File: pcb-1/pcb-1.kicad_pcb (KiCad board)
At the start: 2 copper layers, 131 x 74 mm, 8 parts, among them J1 Raspberry_Pi_2_3, J2 Screw_Terminal_01x03, J3 Conn_01x07_Socket, J4 Screw_Terminal_01x02, J5 Conn_01x02_Socket, U1 Pico, U2 TSR 2-2450

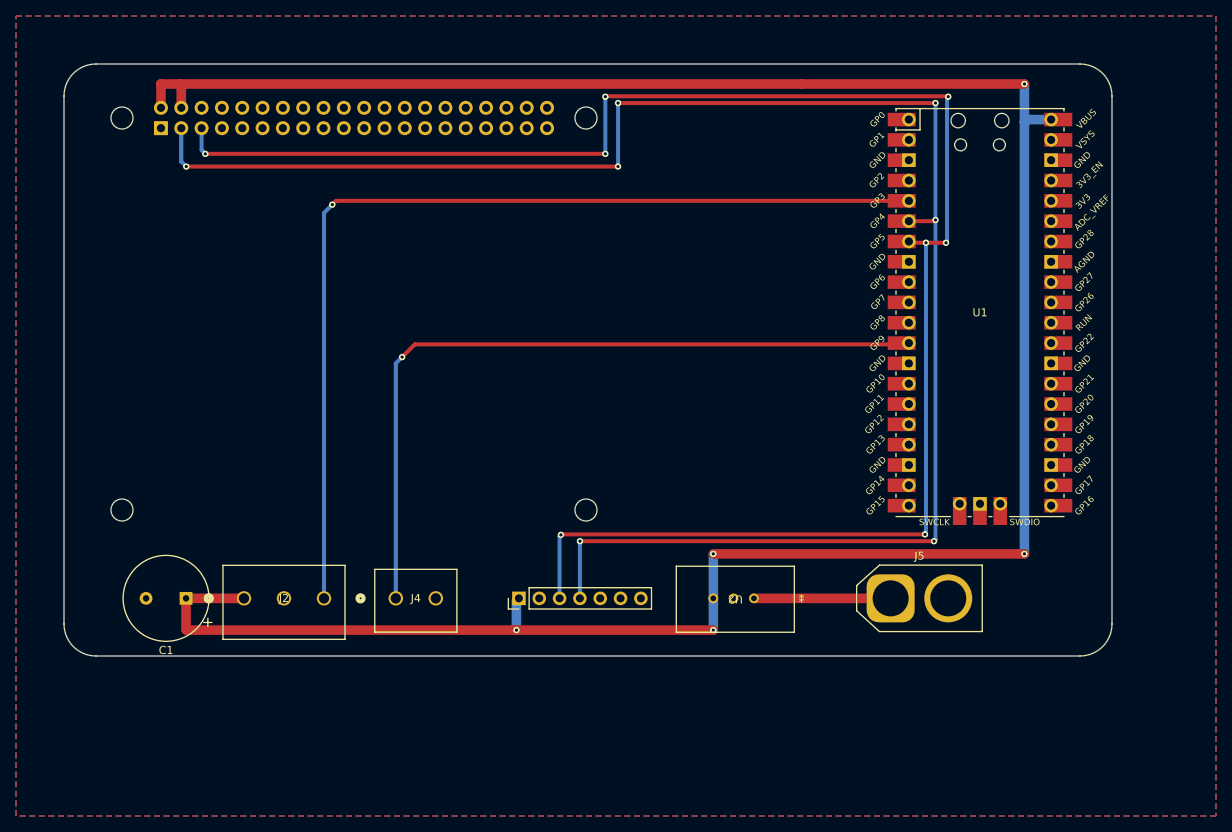
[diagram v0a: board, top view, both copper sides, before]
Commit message: flipped pi - consider rerouting bmx160 so it isn't hanging off the board?
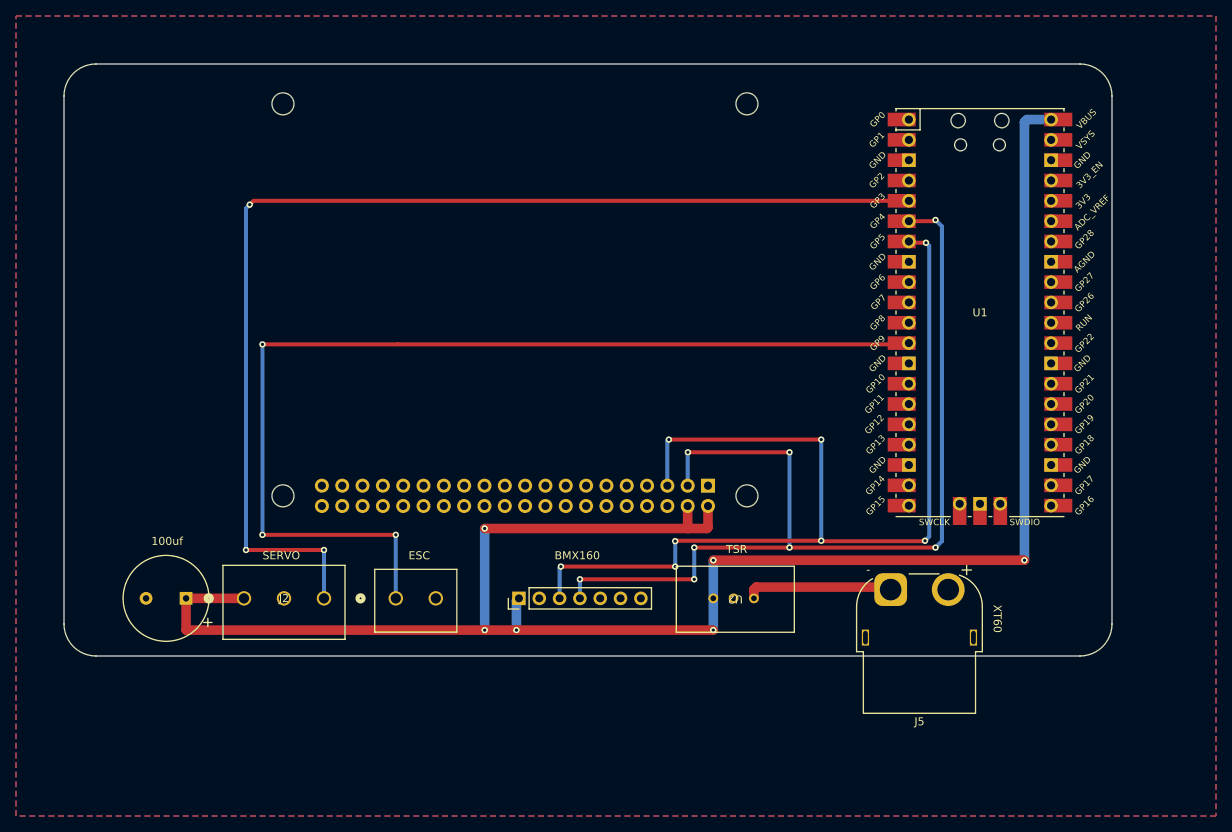
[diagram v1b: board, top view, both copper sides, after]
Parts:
- J5: footprint Connector_AMASS:AMASS_XT60-F_1x02_P7.20mm_Vertical -> Connector_AMASS:AMASS_XT60PW-F_1x02_P7.20mm_Horizontal
- moved J1 51.3 mm to (132.4, 115.0), turned to 180 degrees
- moved J5 1.09 mm to (179.3, 126.7), turned to 180 degrees
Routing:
- net SDA: track 216.3 -> 124.6 mm, vias 7 -> 8
- net SCL: track 216.6 -> 130.2 mm
- net +5V: track 305.8 -> 233.2 mm, vias 5 -> 6
- net ESC: track 94.8 -> 129.5 mm, vias 1 -> 3
- net SERVO: track 121.9 -> 141.7 mm, vias 1 -> 3
- net VCC: track 17.1 -> 18.5 mm
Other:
- board text added: "100uf"
- board text added: "BMX160"
- board text added: "ESC"
- board text added: "SERVO"
- board text added: "TSR"
- board text added: "XT60"

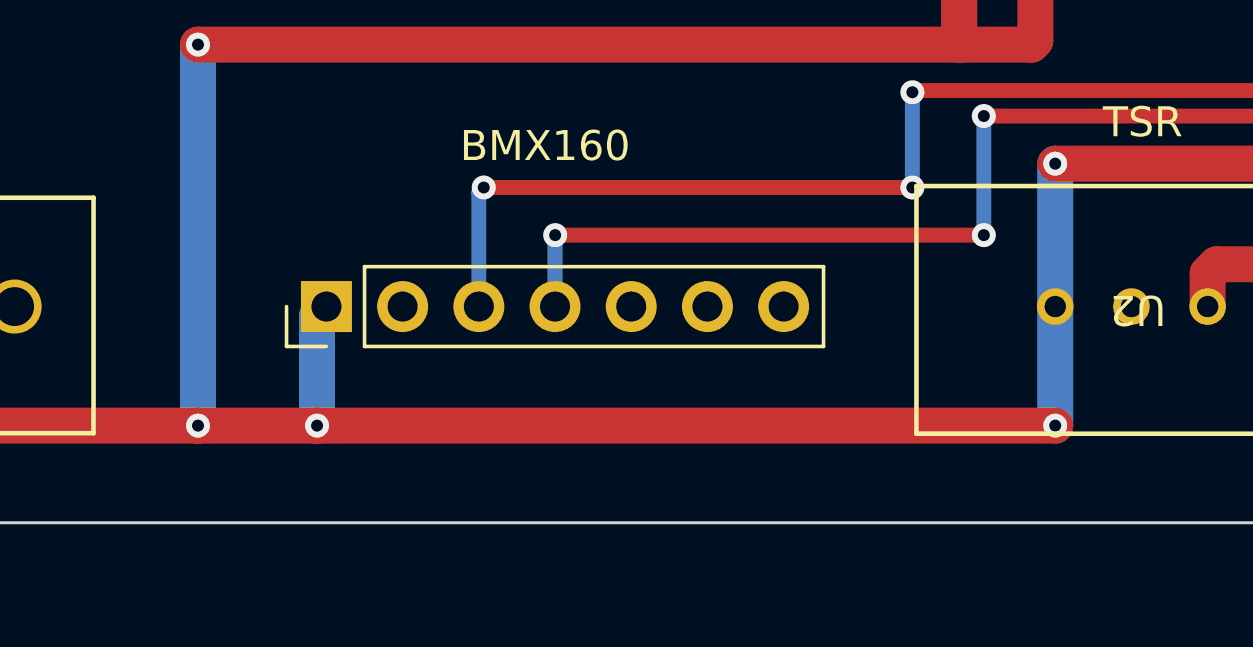
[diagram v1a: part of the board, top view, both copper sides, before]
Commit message: moved trace down a little to avoid thermal relief warning
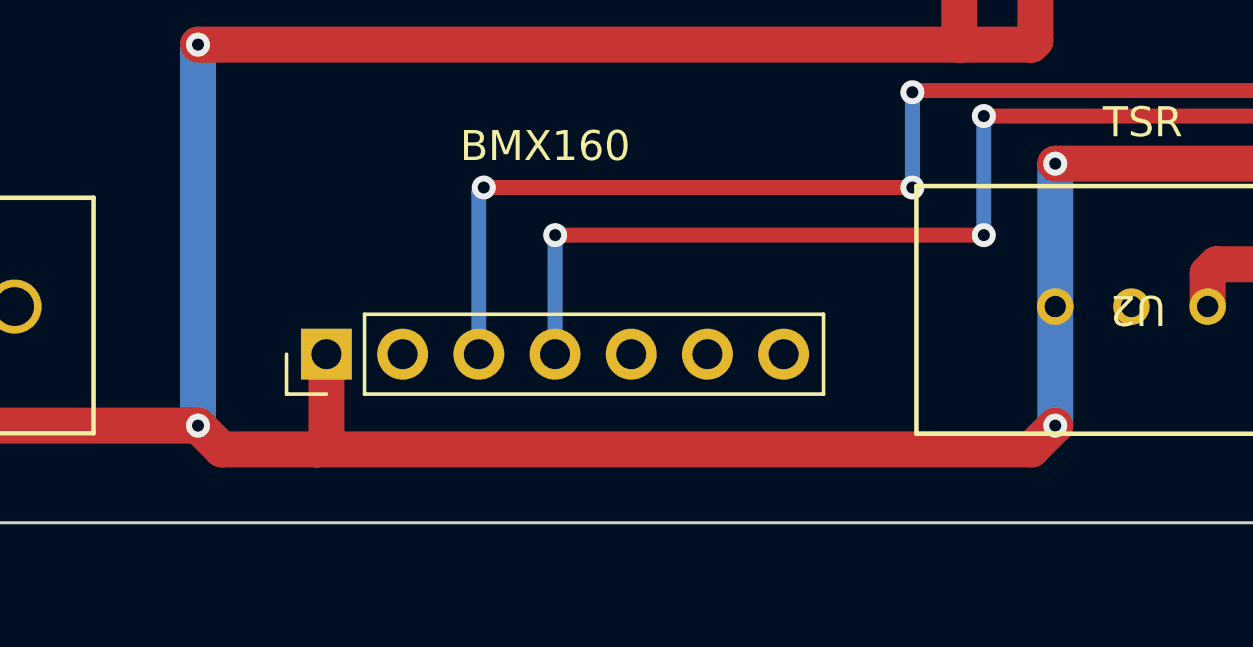
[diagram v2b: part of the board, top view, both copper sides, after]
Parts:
- moved J3 1.59 mm to (132.9, 129.4)
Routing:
- net SCL: track 130.2 -> 131.8 mm
- net SDA: track 124.6 -> 126.2 mm
- net +5V: track 233.2 -> 233.1 mm, vias 6 -> 5
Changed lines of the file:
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@@
   )
   (footprint "Connector_PinHeader_2.54mm:PinHeader_1x07_P2.54mm_Vertical" (layer "F.Cu")
-    (at 132.86875 127.79375 90)
+    (at 132.86875 129.38125 90)
     (descr "Through hole straight pin header, 1x07, 2.54mm pitch, single row")
     (tags "Through hole pin header THT 1x07 2.54mm single row")
@@
   )
   (segment (start 91.258934 127.79375) (end 91.258934 131.740184) (width 1.2) (layer "F.Cu") (net 1))
-  (segment (start 132.55625 131.7625) (end 128.5875 131.7625) (width 1.2) (layer "F.Cu") (net 1))
+  (segment (start 132.86875 132.24375) (end 132.55625 132.55625) (width 1.2) (layer "F.Cu") (net 1))
+  (segment (start 132.86875 129.38125) (end 132.86875 132.24375) (width 1.2) (layer "F.Cu") (net 1))
+  (segment (start 129.38125 132.55625) (end 132.55625 132.55625) (width 1.2) (layer "F.Cu") (net 1))
   (segment (start 153.9875 119.0625) (end 128.5875 119.0625) (width 1.2) (layer "F.Cu") (net 1))
   (segment (start 153.96 119.035) (end 153.96 116.25) (width 1.2) (layer "F.Cu") (net 1))
@@
   (segment (start 156.5 116.25) (end 156.5 118.93125) (width 1.2) (layer "F.Cu") (net 1))
   (segment (start 156.5 118.93125) (end 156.36875 119.0625) (width 1.2) (layer "F.Cu") (net 1))
+  (segment (start 128.5875 131.7625) (end 129.38125 132.55625) (width 1.2) (layer "F.Cu") (net 1))
   (segment (start 128.5875 131.7625) (end 91.28125 131.7625) (width 1.2) (layer "F.Cu") (net 1))
-  (segment (start 157.1625 131.7625) (end 132.55625 131.7625) (width 1.2) (layer "F.Cu") (net 1))
+  (segment (start 156.36875 132.55625) (end 157.1625 131.7625) (width 1.2) (layer "F.Cu") (net 1))
   (segment (start 156.36875 119.0625) (end 153.9875 119.0625) (width 1.2) (layer "F.Cu") (net 1))
+  (segment (start 132.55625 132.55625) (end 156.36875 132.55625) (width 1.2) (layer "F.Cu") (net 1))
   (via (at 157.1625 131.7625) (size 0.8) (drill 0.4) (layers "F.Cu" "B.Cu") (net 1))
   (via (at 128.5875 119.0625) (size 0.8) (drill 0.4) (layers "F.Cu" "B.Cu") (net 1))
@@
   (via (at 196.05625 123.03125) (size 0.8) (drill 0.4) (layers "F.Cu" "B.Cu") (net 1))
   (via (at 157.1625 123.03125) (size 0.8) (drill 0.4) (layers "F.Cu" "B.Cu") (net 1))
-  (via (at 132.55625 131.7625) (size 0.8) (drill 0.4) (layers "F.Cu" "B.Cu") (net 1))
   (segment (start 196.05625 68.2625) (end 196.37375 67.945) (width 1.2) (layer "B.Cu") (net 1))
   (segment (start 128.5875 119.0625) (end 128.5875 131.7625) (width 1.2) (layer "B.Cu") (net 1))
-  (segment (start 132.55625 128.10625) (end 132.86875 127.79375) (width 1.2) (layer "B.Cu") (net 1))
   (segment (start 196.37375 67.945) (end 199.39 67.945) (width 1.2) (layer "B.Cu") (net 1))
   (segment (start 157.1625 127.79375) (end 157.1625 131.7625) (width 1.2) (layer "B.Cu") (net 1))
   (segment (start 157.1625 127.79375) (end 157.1625 123.03125) (width 1.2) (layer "B.Cu") (net 1))
   (segment (start 196.05625 123.03125) (end 196.05625 68.2625) (width 1.2) (layer "B.Cu") (net 1))
-  (segment (start 132.55625 131.7625) (end 132.55625 128.10625) (width 1.2) (layer "B.Cu") (net 1))
   (segment (start 138.1125 123.825) (end 152.4 123.825) (width 0.5) (layer "F.Cu") (net 24))
   (segment (start 152.45625 120.59375) (end 170.65625 120.59375) (width 0.5) (layer "F.Cu") (net 24))
@@
   (via (at 152.4 120.65) (size 0.8) (drill 0.4) (layers "F.Cu" "B.Cu") (net 24))
   (segment (start 170.65625 107.95) (end 170.65625 120.59375) (width 0.5) (layer "B.Cu") (net 24))
+  (segment (start 137.94875 123.98875) (end 138.1125 123.825) (width 0.5) (layer "B.Cu") (net 24))
   (segment (start 151.42 108.13625) (end 151.60625 107.95) (width 0.5) (layer "B.Cu") (net 24))
-  (segment (start 138.1125 123.825) (end 137.94875 123.98875) (width 0.5) (layer "B.Cu") (net 24))
+  (segment (start 137.94875 129.38125) (end 137.94875 123.98875) (width 0.5) (layer "B.Cu") (net 24))
   (segment (start 152.4 123.825) (end 152.4 120.65) (width 0.5) (layer "B.Cu") (net 24))
   (segment (start 184.15 83.74375) (end 183.75 83.34375) (width 0.5) (layer "B.Cu") (net 24))
@@
   (segment (start 184.15 120.069651) (end 184.15 83.74375) (width 0.5) (layer "B.Cu") (net 24))
   (segment (start 183.625901 120.59375) (end 184.15 120.069651) (width 0.5) (layer "B.Cu") (net 24))
-  (segment (start 137.94875 123.98875) (end 137.94875 127.79375) (width 0.5) (layer "B.Cu") (net 24))
   (segment (start 184.94375 80.5) (end 184.79875 80.645) (width 0.5) (layer "F.Cu") (net 25))
   (segment (start 154.78125 121.44375) (end 166.6875 121.44375) (width 0.5) (layer "F.Cu") (net 25))
@@
   (segment (start 153.96 113.71) (end 153.96 109.565) (width 0.5) (layer "B.Cu") (net 25))
   (segment (start 153.96 109.565) (end 153.9875 109.5375) (width 0.5) (layer "B.Cu") (net 25))
+  (segment (start 140.48875 125.4175) (end 140.49375 125.4125) (width 0.5) (layer "B.Cu") (net 25))
   (segment (start 185.7375 120.65) (end 185.7375 81.29375) (width 0.5) (layer "B.Cu") (net 25))
   (segment (start 185.7375 81.29375) (end 184.94375 80.5) (width 0.5) (layer "B.Cu") (net 25))
-  (segment (start 140.48875 127.79375) (end 140.48875 125.4175) (width 0.5) (layer "B.Cu") (net 25))
-  (segment (start 140.48875 125.4175) (end 140.49375 125.4125) (width 0.5) (layer "B.Cu") (net 25))
+  (segment (start 140.48875 129.38125) (end 140.48875 125.4175) (width 0.5) (layer "B.Cu") (net 25))
   (segment (start 184.94375 121.44375) (end 185.7375 120.65) (width 0.5) (layer "B.Cu") (net 25))
   (segment (start 154.78125 125.4125) (end 154.78125 121.44375) (width 0.5) (layer "B.Cu") (net 25))

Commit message: updates to pcb
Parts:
- added BMX160-Drawing: LOGO, LOGO, F.Cu at (140.6, 126.3)
- moved J3 1.12 mm to (132.9, 130.5)
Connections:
- J3 pad 1: +5V -> unconnected-(J3-Pin_1-Pad1)
- J3 pad 2: GND -> unconnected-(J3-Pin_2-Pad2)
- J3 pad 3: SCL -> GND
- J3 pad 5: GND -> SCL
- J3 pad 6: unconnected-(J3-Pin_6-Pad6) -> GND
- J3 pad 7: unconnected-(J3-Pin_7-Pad7) -> +5V
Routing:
- net +5V: track 233.1 -> 235.5 mm
- net SCL: track 131.8 -> 129.5 mm, vias 8 -> 6
- net SDA: track 126.2 -> 128.3 mm, vias 8 -> 6
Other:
- board text removed: "100uf"
